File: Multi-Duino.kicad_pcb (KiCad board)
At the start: 4 copper layers, 68.6 x 53.3 mm, 67 parts, among them J1 M20-9980345, J10 Micro_SD_Card_Det1, J2 M20-9980245, J3 M20-9980345, J4 PPTC101LFBN-RC, J5 PPTC081LFBN-RC, J6 PPTC061LFBN-RC, J7 PPTC081LFBN-RC, J8 USB_C_Receptacle_USB2.0_16P, Q1 FDN340P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

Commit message: Update Multiduino v2 design
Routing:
- net IO9: track 0.00 -> 39.2 mm
- net IO6: track 0.00 -> 38.2 mm
- net IO7: track 0.00 -> 38.2 mm
- net IO5: track 0.00 -> 38.1 mm
- net IO8: track 0.00 -> 37.6 mm
- net MOSI: track 0.00 -> 16.5 mm
- net SCK: track 0.00 -> 16.0 mm

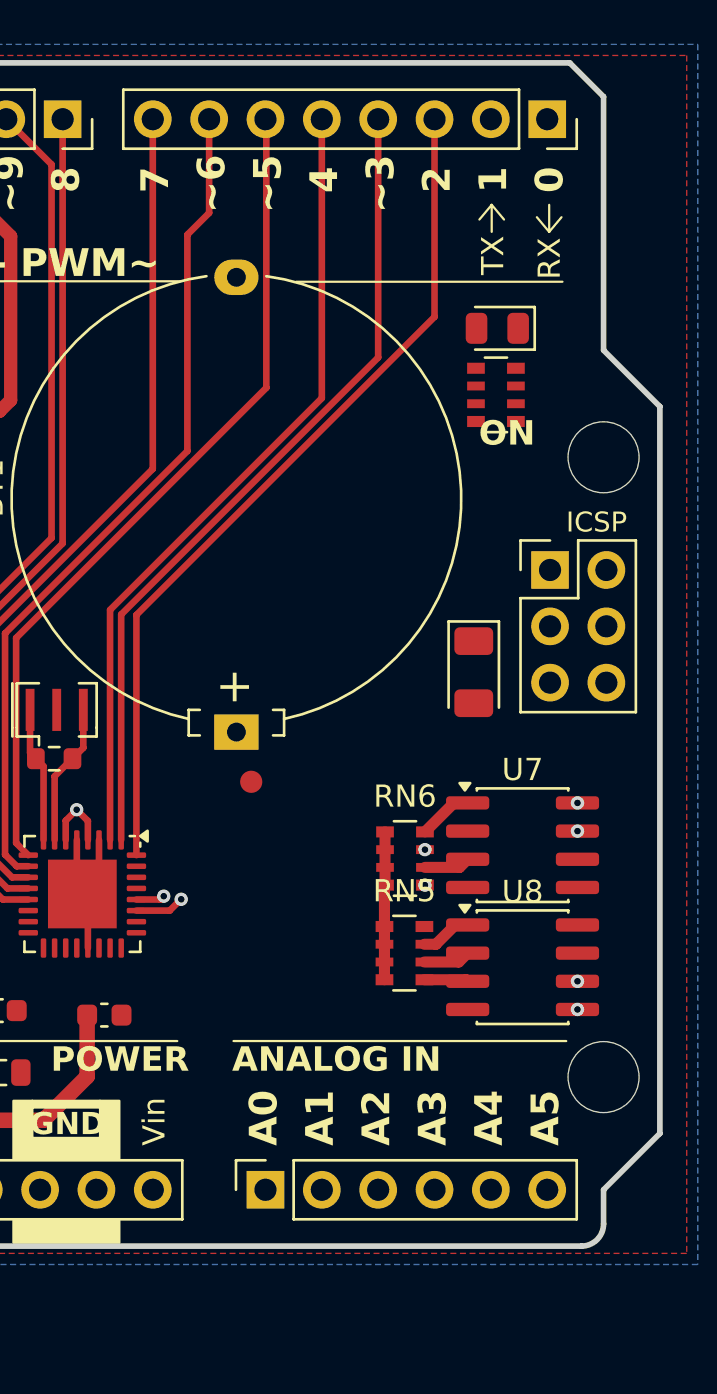
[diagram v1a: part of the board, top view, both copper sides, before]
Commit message: Update Multiduino v2 design
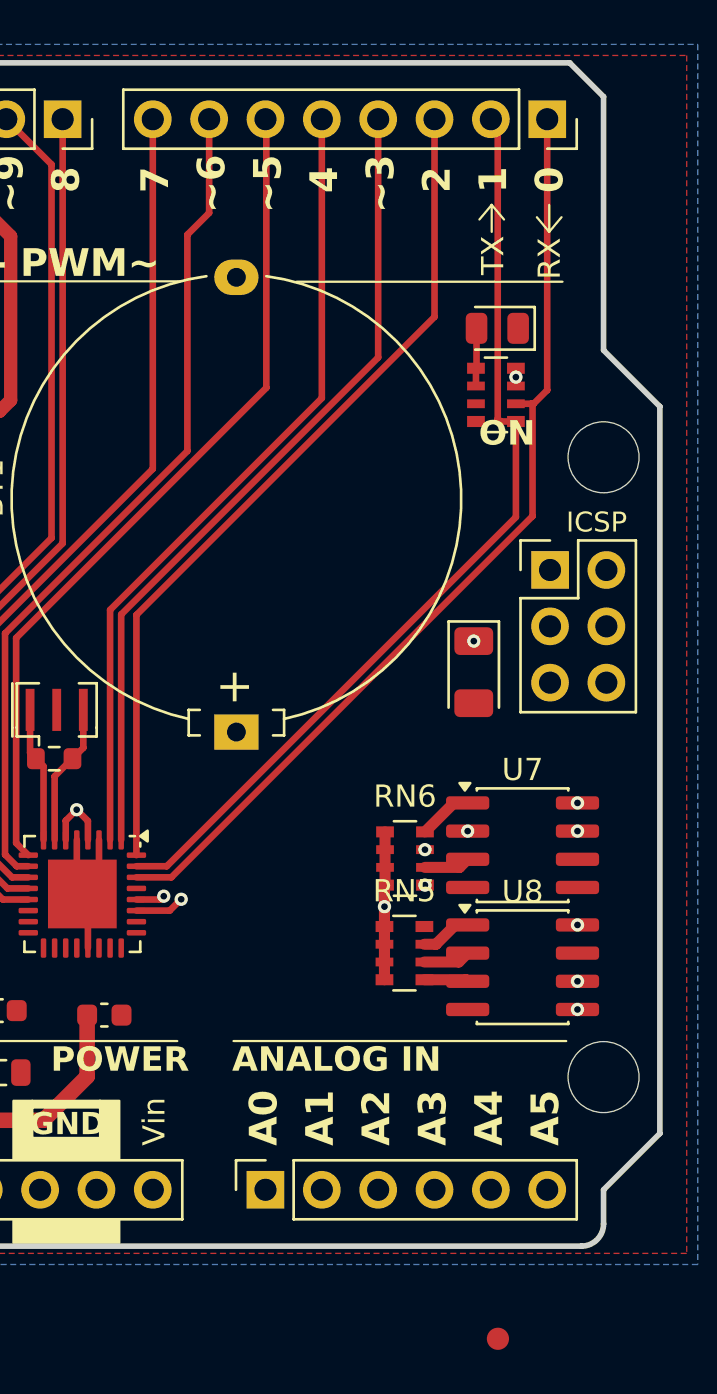
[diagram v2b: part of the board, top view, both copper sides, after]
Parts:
- moved FID2 27.5 mm to (175.5, 135.8)
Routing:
- net IO0: track 0.00 -> 43.6 mm
- net IO1: track 0.00 -> 42.4 mm
- net Net-(D7-A): track 0.00 -> 2.61 mm
- net +5V: track 50.6 -> 51.4 mm, vias 13 -> 18
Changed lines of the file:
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@@
 	(footprint "Fiducial:Fiducial_1mm_Mask2mm"
 		(layer "F.Cu")
-		(at 164.3681 110.7416)
+		(at 175.49 135.85)
 		(descr "Circular Fiducial, 1mm bare copper, 2mm soldermask opening (Level A)")
 		(tags "fiducial")
@@
 	(segment
 		(start 170.375 117.265)
-		(end 170.375 115.425)
+		(end 170.375 116.37)
 		(width 0.5)
 		(layer "F.Cu")
@@
 	)
 	(segment
+		(start 170.375 116.37)
+		(end 170.375 115.425)
+		(width 0.5)
+		(layer "F.Cu")
+		(net 2)
+	)
+	(segment
 		(start 156.5 112)
 		(end 157.0061 112.5061)
@@
 	)
 	(segment
+		(start 176.3 92.5)
+		(end 176.3 92.9)
+		(width 0.3)
+		(layer "F.Cu")
+		(net 2)
+	)
+	(segment
 		(start 131.7126 99.44)
 		(end 131.7126 98.7526)
@@
 	)
 	(segment
+		(start 176.3 92.1)
+		(end 176.3 92.5)
+		(width 0.3)
+		(layer "F.Cu")
+		(net 2)
+	)
+	(segment
 		(start 141.2511 92.3)
 		(end 141.2511 92.7036)
@@
 		(width 0.7)
 		(layer "F.Cu")
+		(net 2)
+	)
+	(via
+		(at 179.075 117.195)
+		(size 0.6)
+		(drill 0.3)
+		(layers "F.Cu" "B.Cu")
 		(net 2)
 	)
@@
 	)
 	(via
+		(at 174.4 104.4)
+		(size 0.6)
+		(drill 0.3)
+		(layers "F.Cu" "B.Cu")
+		(net 2)
+	)
+	(via
 		(at 141.2511 106.5976)
 		(size 0.6)
@@
 	)
 	(via
+		(at 176.3 92.5)
+		(size 0.6)
+		(drill 0.3)
+		(layers "F.Cu" "B.Cu")
+		(net 2)
+	)
+	(via
 		(at 156.5 112)
 		(size 0.6)
@@
 	)
 	(via
+		(at 174.125 112.965)
+		(size 0.6)
+		(drill 0.3)
+		(layers "F.Cu" "B.Cu")
+		(net 2)
+	)
+	(via
+		(at 170.375 116.37)
+		(size 0.6)
+		(drill 0.3)
+		(layers "F.Cu" "B.Cu")
+		(net 2)
+	)
+	(via
 		(at 141.2511 92.3)
 		(size 0.6)
@@
 		(layer "F.Cu")
 		(net 11)
+	)
+	(segment
+		(start 174.5 92.9)
+		(end 174.5 92.1)
+		(width 0.3)
+		(layer "F.Cu")
+		(net 19)
+	)
+	(segment
+		(start 174.525 90.3)
+		(end 174.525 92.075)
+		(width 0.3)
+		(layer "F.Cu")
+		(net 19)
+	)
+	(segment
+		(start 174.525 92.075)
+		(end 174.5 92.1)
+		(width 0.3)
+		(layer "F.Cu")
+		(net 19)
 	)
 	(segment
@@
 	)
 	(segment
+		(start 177.05 93.75)
+		(end 177 93.7)
+		(width 0.3)
+		(layer "F.Cu")
+		(net 43)
+	)
+	(segment
+		(start 177 93.7)
+		(end 176.3 93.7)
+		(width 0.3)
+		(layer "F.Cu")
+		(net 43)
+	)
+	(segment
+		(start 160.768506 115.0486)
+		(end 177.05 98.767106)
+		(width 0.3)
+		(layer "F.Cu")
+		(net 43)
+	)
+	(segment
+		(start 177.7111 80.8736)
+		(end 177.7111 93.0889)
+		(width 0.3)
+		(layer "F.Cu")
+		(net 43)
+	)
+	(segment
+		(start 159.1936 115.0486)
+		(end 160.768506 115.0486)
+		(width 0.3)
+		(layer "F.Cu")
+		(net 43)
+	)
+	(segment
+		(start 177.05 98.767106)
+		(end 177.05 93.75)
+		(width 0.3)
+		(layer "F.Cu")
+		(net 43)
+	)
+	(segment
+		(start 177.1 93.7)
+		(end 177 93.7)
+		(width 0.3)
+		(layer "F.Cu")
+		(net 43)
+	)
+	(segment
+		(start 177.7111 93.0889)
+		(end 177.1 93.7)
+		(width 0.3)
+		(layer "F.Cu")
+		(net 43)
+	)
+	(segment
+		(start 159.1936 114.5486)
+		(end 160.5614 114.5486)
+		(width 0.3)
+		(layer "F.Cu")
+		(net 44)
+	)
+	(segment
+		(start 176.3 98.81)
+		(end 176.3 94.5)
+		(width 0.3)
+		(layer "F.Cu")
+		(net 44)
+	)
+	(segment
+		(start 175.6 94.5)
+		(end 176.3 94.5)
+		(width 0.3)
+		(layer "F.Cu")
+		(net 44)
+	)
+	(segment
+		(start 160.5614 114.5486)
+		(end 176.3 98.81)
+		(width 0.3)
+		(layer "F.Cu")
+		(net 44)
+	)
+	(segment
+		(start 175.48 94.38)
+		(end 175.6 94.5)
+		(width 0.3)
+		(layer "F.Cu")
+		(net 44)
+	)
+	(segment
+		(start 175.48 81.1825)
+		(end 175.48 94.38)
+		(width 0.3)
+		(layer "F.Cu")
+		(net 44)
+	)
+	(segment
+		(start 175.1711 80.8736)
+		(end 175.48 81.1825)
+		(width 0.3)
+		(layer "F.Cu")
+		(net 44)
+	)
+	(segment

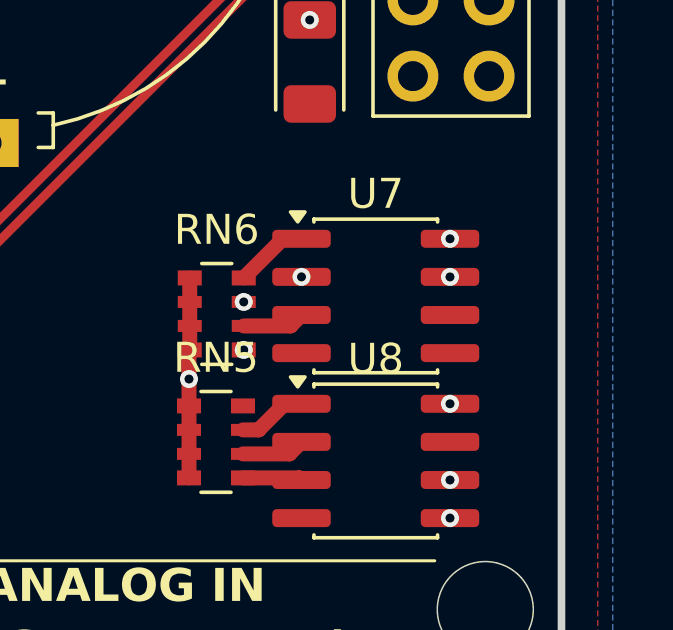
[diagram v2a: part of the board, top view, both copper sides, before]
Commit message: Update Multiduino v2 design
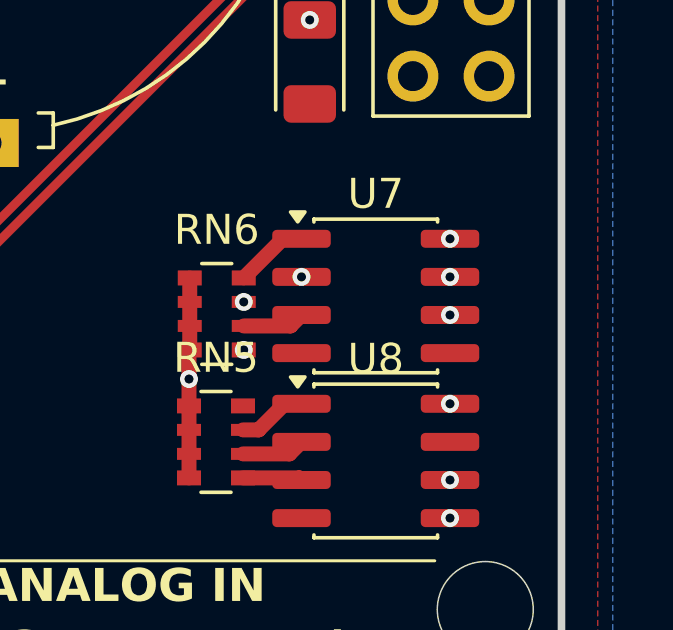
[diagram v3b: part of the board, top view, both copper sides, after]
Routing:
- net Net-(BT1-+): track 0.00 -> 17.8 mm, vias 0 -> 1
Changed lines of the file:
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@@
 		(net 98)
+	)
+	(via
+		(at 179.075 114.235)
+		(size 0.6)
+		(drill 0.3)
+		(layers "F.Cu" "B.Cu")
+		(net 101)
+	)
+	(segment
+		(start 179.075 114.235)
+		(end 173.34 108.5)
+		(width 0.5)
+		(layer "In1.Cu")
+		(net 101)
+	)
+	(segment
+		(start 173.34 108.5)
+		(end 163.7 108.5)
+		(width 0.5)
+		(layer "In1.Cu")
+		(net 101)
 	)
 	(zone

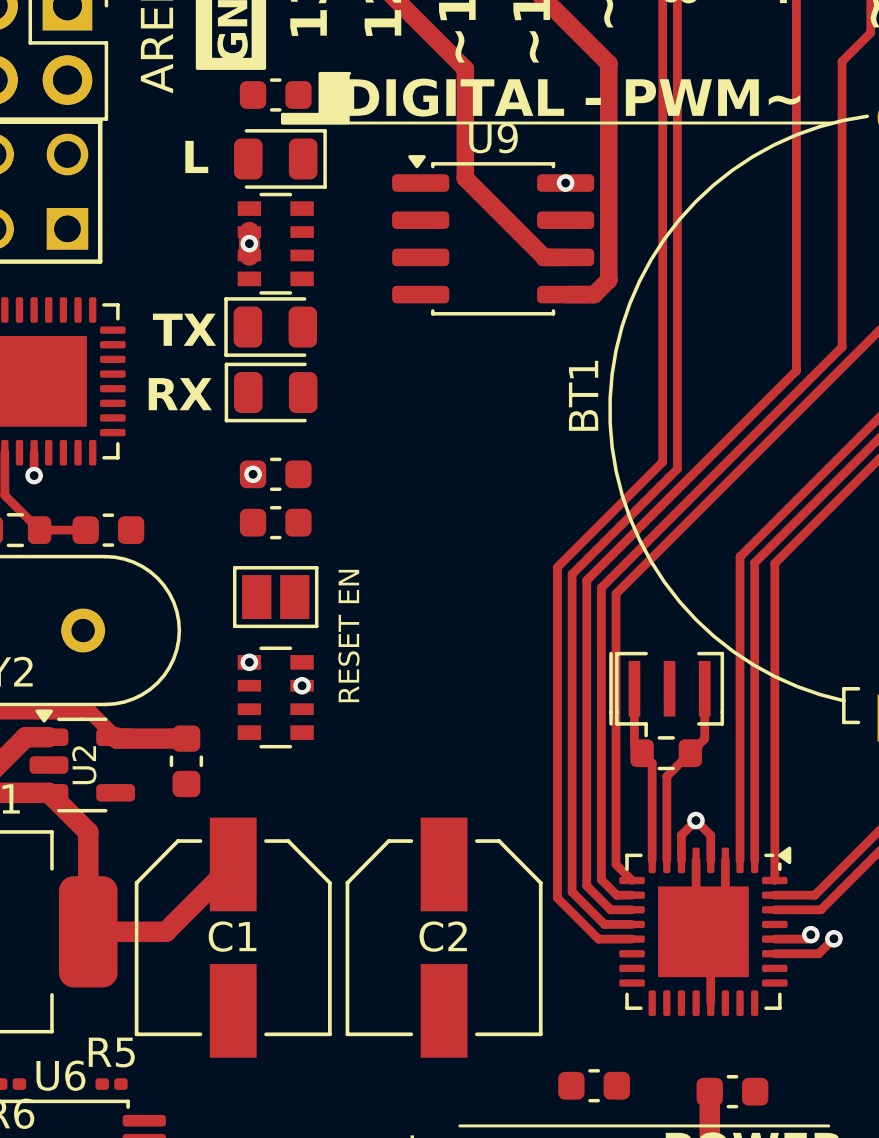
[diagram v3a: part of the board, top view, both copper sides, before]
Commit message: Update Multiduino v2 design
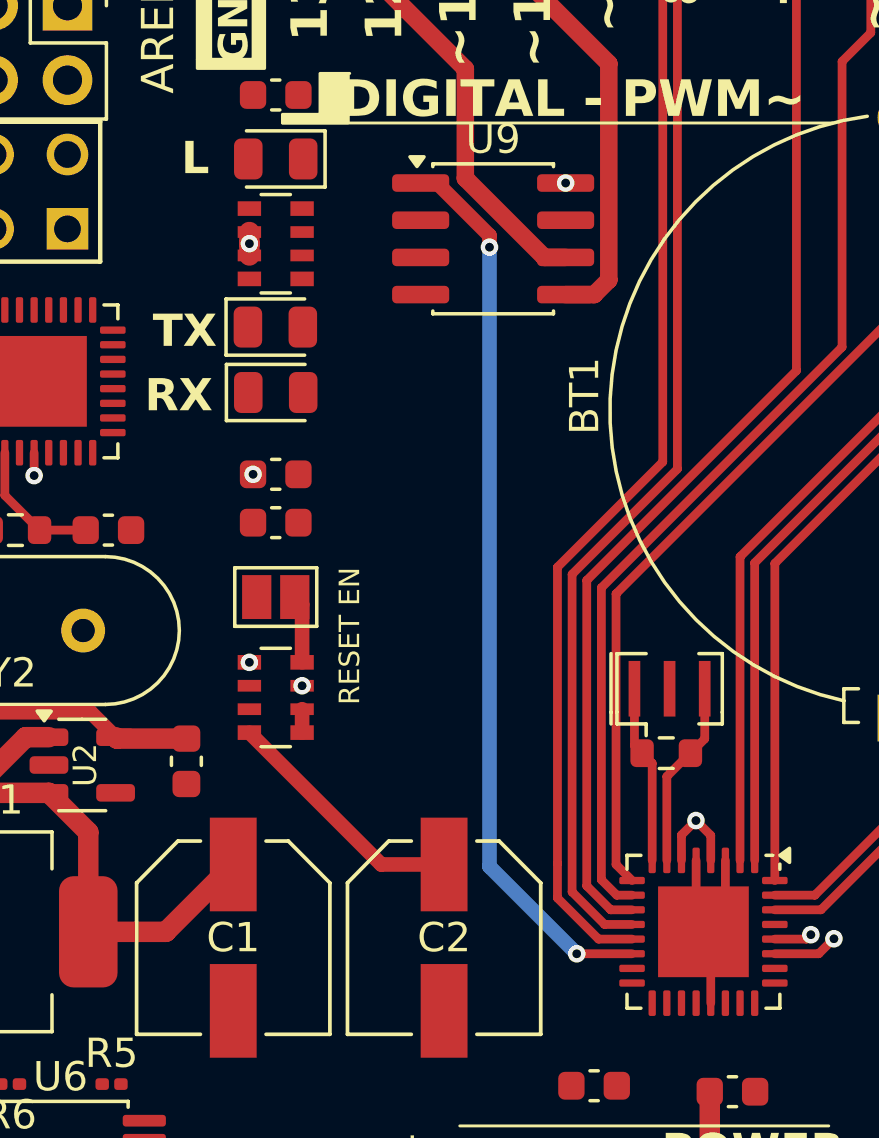
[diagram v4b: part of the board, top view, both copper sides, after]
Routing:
- net SS: track 0.00 -> 30.7 mm, vias 0 -> 2
- net VCC: track 0.00 -> 8.51 mm
- net RESET: track 8.40 -> 10.7 mm
- net CMP: track 0.00 -> 0.80 mm
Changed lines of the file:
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@@
+	)
+	(segment
+		(start 141.2511 108.9976)
+		(end 145.7535 113.5)
+		(width 0.5)
+		(layer "F.Cu")
+		(net 3)
+	)
+	(segment
+		(start 145.7535 113.5)
+		(end 147.9 113.5)
+		(width 0.5)
+		(layer "F.Cu")
+		(net 3)
 	)
 	(segment
@@
 	)
 	(segment
+		(start 143.0511 106.5976)
+		(end 143.0511 104.6186)
+		(width 0.5)
+		(layer "F.Cu")
+		(net 6)
+	)
+	(segment
+		(start 143.0511 104.6186)
+		(end 142.8011 104.3686)
+		(width 0.5)
+		(layer "F.Cu")
+		(net 6)
+	)
+	(segment
 		(start 132.4361 102.0826)
 		(end 130.9881 102.0826)
@@
 	)
 	(segment
+		(start 152.4314 116.5486)
+		(end 152.43 116.55)
+		(width 0.3)
+		(layer "F.Cu")
+		(net 37)
+	)
+	(segment
+		(start 149.45 92.022316)
+		(end 149.45 92.42)
+		(width 0.5)
+		(layer "F.Cu")
+		(net 37)
+	)
+	(segment
+		(start 154.3186 116.5486)
+		(end 152.4314 116.5486)
+		(width 0.3)
+		(layer "F.Cu")
+		(net 37)
+	)
+	(segment
+		(start 147.657684 90.23)
+		(end 149.45 92.022316)
+		(width 0.5)
+		(layer "F.Cu")
+		(net 37)
+	)
+	(segment
+		(start 147.1 90.23)
+		(end 147.657684 90.23)
+		(width 0.5)
+		(layer "F.Cu")
+		(net 37)
+	)
+	(via
+		(at 152.43 116.55)
+		(size 0.6)
+		(drill 0.3)
+		(layers "F.Cu" "B.Cu")
+		(net 37)
+	)
+	(via
+		(at 149.45 92.42)
+		(size 0.6)
+		(drill 0.3)
+		(layers "F.Cu" "B.Cu")
+		(net 37)
+	)
+	(segment
+		(start 149.45 113.57)
+		(end 152.43 116.55)
+		(width 0.5)
+		(layer "B.Cu")
+		(net 37)
+	)
+	(segment
+		(start 149.45 92.42)
+		(end 149.45 113.57)
+		(width 0.5)
+		(layer "B.Cu")
+		(net 37)
+	)
+	(segment
 		(start 162.4711 85.0989)
 		(end 162.4711 80.8736)
@@
 	)
 	(segment
+		(start 143.0511 108.9976)
+		(end 143.0511 108.1976)
+		(width 0.5)
+		(layer "F.Cu")
+		(net 60)
+	)
+	(segment
